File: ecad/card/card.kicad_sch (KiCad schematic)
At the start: 52 parts, among them J1 Conn_01x03_Pin, J2 USB4105-GF-A, SW1 SW_Push, SW2 SW_Push, U1 W25Q128JVS, U2 RP2350_80QFN, U3 MCP23017_SO, U4 NCP1117-3.3_SOT223, U5 MCP23017_SO, X1 ABM8-272-T3

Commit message: fixup card labels
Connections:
- net ADDR00: now also U2.25 (GPIO24)
- net ADDR01: now also U2.26 (GPIO25)
- net ADDR02: now also U2.27 (GPIO26)
- net ADDR03: now also U2.28 (GPIO27)
- net ADDR04: now also U2.36 (GPIO28)
- net ADDR05: now also U2.37 (GPIO29)
- net ADDR06: now also U2.38 (GPIO30)
- net ADDR07: now also U2.39 (GPIO31)
- net ADDR08: now also U2.40 (GPIO32)
- net ADDR09: now also U2.42 (GPIO33)
- net ADDR10: now also U2.43 (GPIO34)
- net ADDR11: now also U2.44 (GPIO35)
- net ADDR12: now also U2.45 (GPIO36)
- net ADDR13: now also U2.46 (GPIO37)
- net ADDR14: now also U2.47 (GPIO38)
- net ADDR15: now also U2.48 (GPIO39)
- net BUS00: now also U2.23 (GPIO23)
- net BUS01: now also U2.22 (GPIO22)
- net BUS02: now also U2.21 (GPIO21)
- net BUS03: now also U2.20 (GPIO20)
- net BUS04: now also U2.19 (GPIO19)
- net BUS05: now also U2.18 (GPIO18)
- net BUS06: now also U2.17 (GPIO17)
- net BUS07: now also U2.16 (GPIO16)
- net BUS08: now also U2.14 (GPIO15)
- net BUS09: now also U2.13 (GPIO14)
- net BUS10: now also U2.12 (GPIO13)
- net BUS11: now also U2.11 (GPIO12)
- net BUS12: now also U2.9 (GPIO11)
- net BUS13: now also U2.8 (GPIO10)
- net BUS14: now also U2.7 (GPIO9)
- net BUS15: now also U2.6 (GPIO8)
- net BUS16: now also U2.4 (GPIO7)
- net BUS17: now also U2.3 (GPIO6)
- net BUS18: now also U2.2 (GPIO5)
- net BUS19: now also U2.1 (GPIO4)
- net BUS20: now also JP1.2 (B)
- net BUS21: now also JP4.2 (B)
- net BUS22: now also JP6.2 (B)
- net BUS23: now also JP8.2 (B)
- net DATA0: now also U2.49 (GPIO40_ADC0)
- net DATA1: now also U2.52 (GPIO41_ADC1)
- net DATA2: now also U2.53 (GPIO42_ADC2)
- net DATA3: now also U2.54 (GPIO43_ADC3)
- net DATA4: now also U2.55 (GPIO44_ADC4)
- net DATA5: now also U2.56 (GPIO45_ADC5)
- net DATA6: now also U2.57 (GPIO46_ADC6)
- net DATA7: now also U2.58 (GPIO47_ADC7)
- net EXT00: now also U3.1 (GPB0)
- net EXT01: now also U3.2 (GPB1)
- net EXT02: now also U3.3 (GPB2)
- net EXT03: now also U3.4 (GPB3)
- net EXT04: now also U3.5 (GPB4)
- net EXT05: now also U3.6 (GPB5)
- net EXT06: now also U3.7 (GPB6)
- net EXT07: now also U3.8 (GPB7)
- net EXT08: now also U3.21 (GPA0)
- net EXT09: now also U3.22 (GPA1)
- net EXT10: now also U3.23 (GPA2)
- net EXT11: now also U3.24 (GPA3)
- net EXT12: now also U3.25 (GPA4)
- net EXT13: now also U3.26 (GPA5)
- net EXT14: now also U3.27 (GPA6)
- net EXT15: now also U3.28 (GPA7)
- net EXT16: now also U5.1 (GPB0)
- net EXT17: now also U5.2 (GPB1)
- net EXT18: now also U5.3 (GPB2)
- net EXT19: now also U5.4 (GPB3)
- net EXT20: now also U5.5 (GPB4)
- net EXT21: now also U5.6 (GPB5)
- net EXT22: now also U5.7 (GPB6)
- net EXT23: now also U5.8 (GPB7)
- net EXT24: now also U5.21 (GPA0)
- net EXT25: now also U5.22 (GPA1)
- net EXT26: now also U5.23 (GPA2)
- net EXT27: now also U5.24 (GPA3)
- net EXT28: now also U5.25 (GPA4)
- net EXT29: now also U5.26 (GPA5)
- net EXT30: now also U5.27 (GPA6)
- net EXT31: now also U5.28 (GPA7)
- net I2C0_SCL: now also JP5.2 (B), U3.12 (SCK)
- net I2C0_SDA: now also JP7.2 (B), U3.13 (SDA)
- net I2C1_SCL: now also JP2.2 (B), U5.12 (SCK)
- net I2C1_SDA: now also JP3.2 (B), U5.13 (SDA)
- net QSPI_SS: now also R3.2, U1.1 (~{CS}), U2.75 (QSPI_SS)
- net USB_D+: now also J2.A6 (DP1), J2.B6 (DP2), R5.2
- net USB_D-: now also J2.A7 (DN1), J2.B7 (DN2), R6.2
- net VREG_LX: now also L1.2, U2.63 (VREG_LX)
- net ~{RESET}: now also R7.1, SW2.2, U2.35 (RUN), U3.18 (~{RESET}), U5.18 (~{RESET})
- net ~{USB_BOOT}: now also R3.1, SW1.2
- net VREG_AVDD: now reaches C7.1, R2.2, U2.61 (VREG_AVDD)

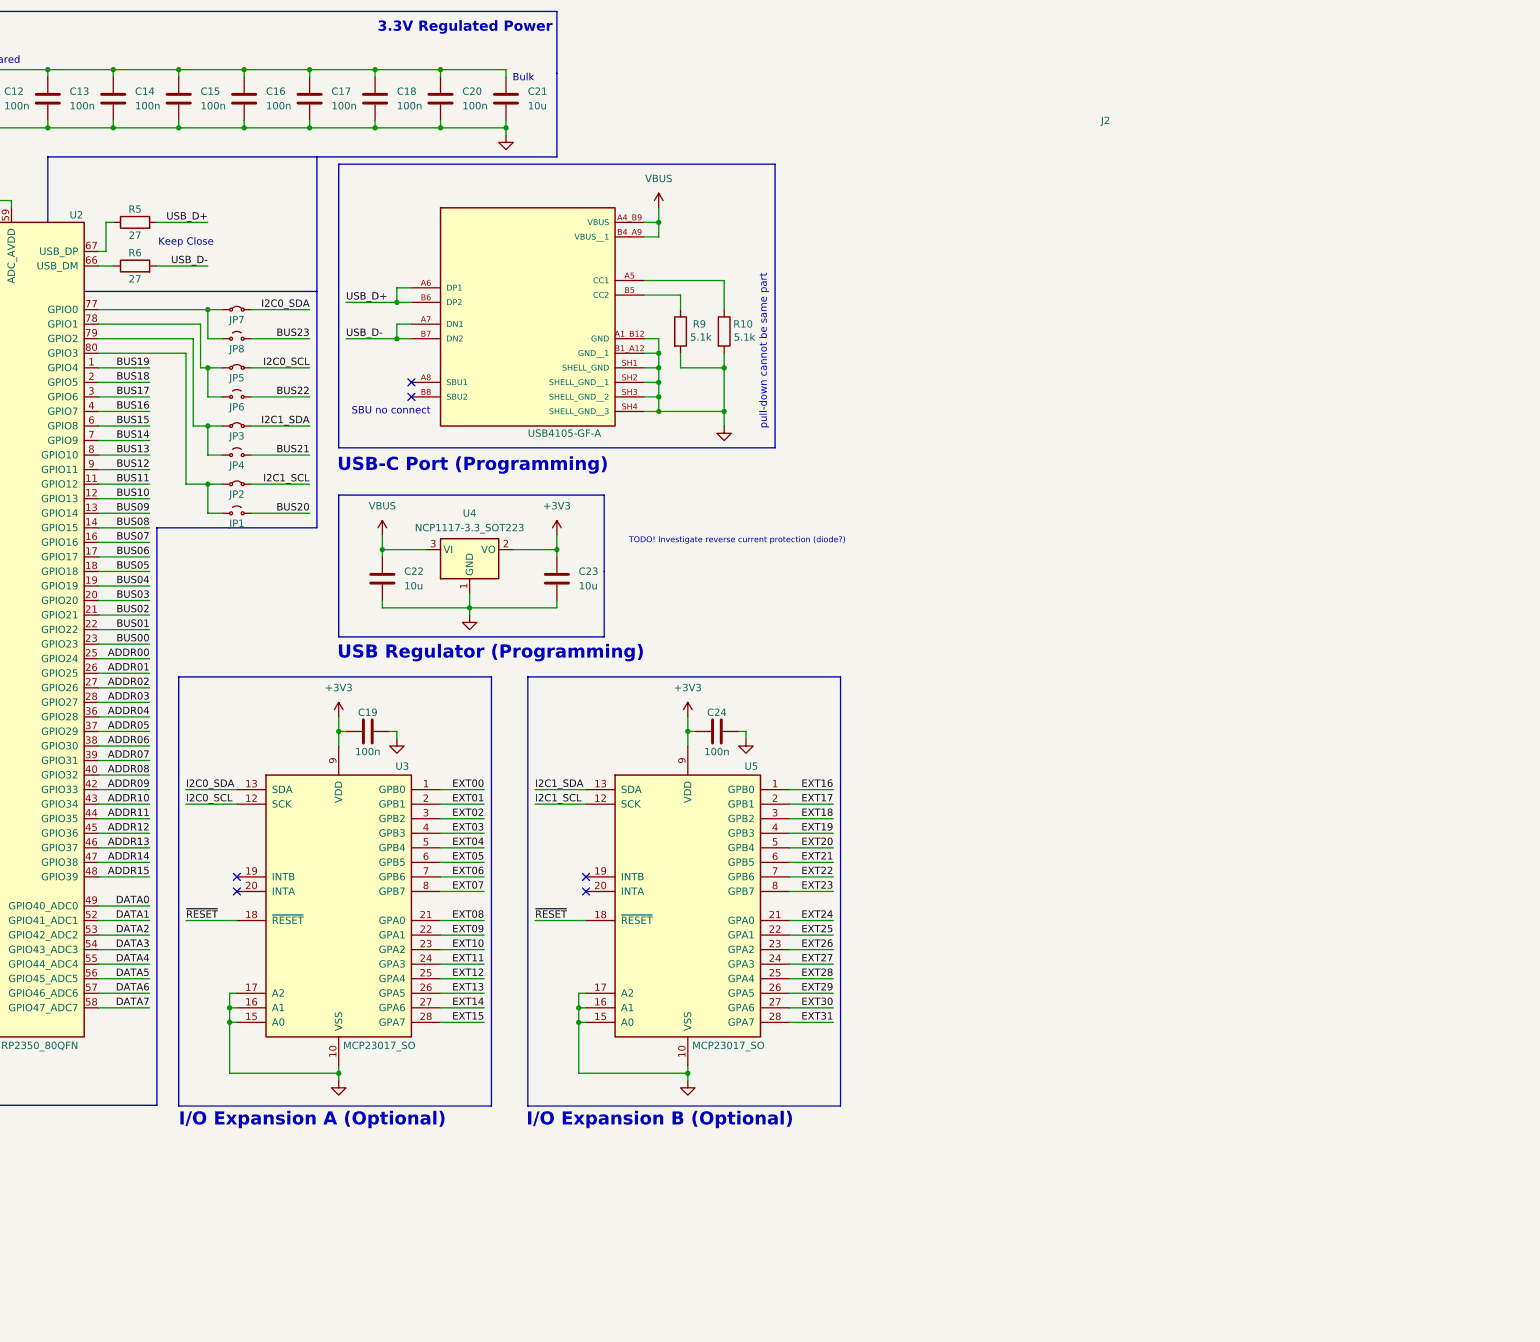
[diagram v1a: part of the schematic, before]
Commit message: integrate edge card symbol into card
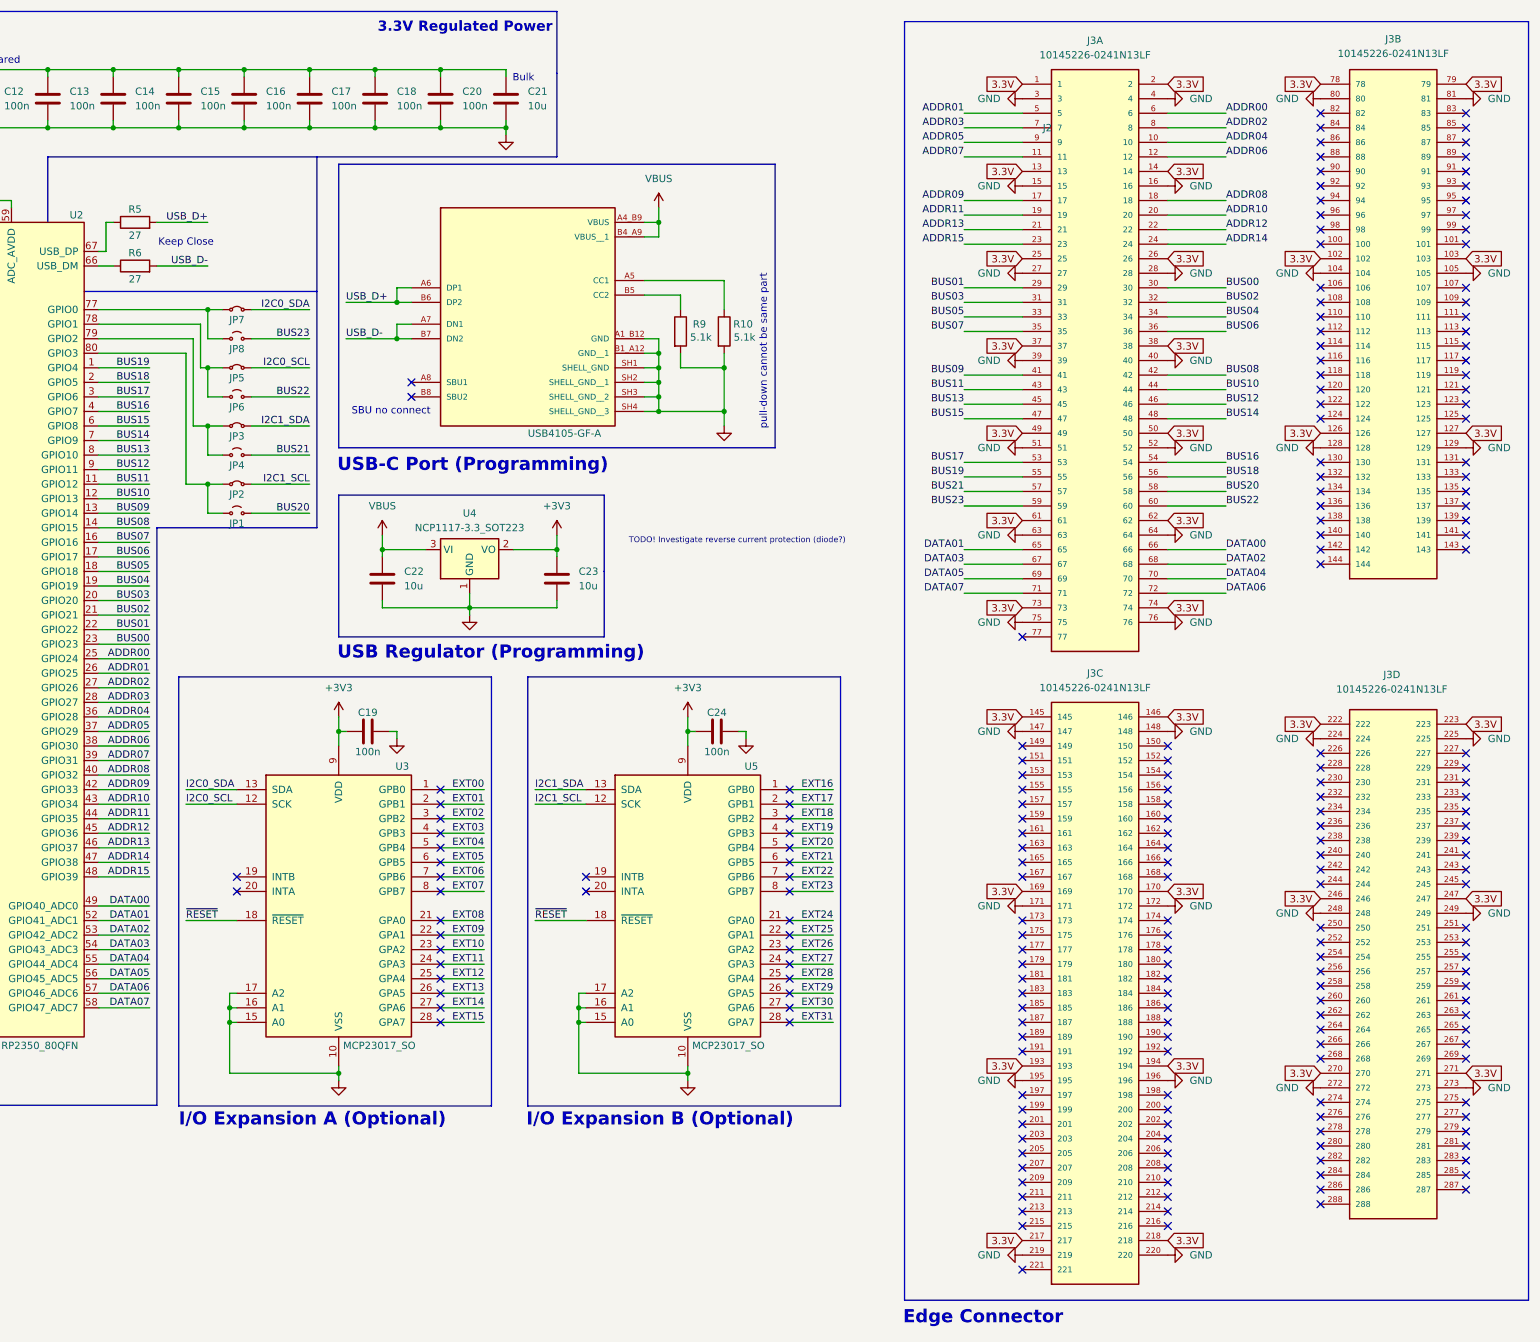
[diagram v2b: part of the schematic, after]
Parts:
- added J3: 10145226-0241N13LF, 10145226-0241N13LF:AMPHENOL_10145226-0241N13LF, symbol Project_Library:10145226-0241N13LF
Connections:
- net ADDR00: now also J3.6
- net ADDR01: now also J3.5
- net ADDR02: now also J3.8
- net ADDR03: now also J3.7
- net ADDR04: now also J3.10
- net ADDR05: now also J3.9
- net ADDR06: now also J3.12
- net ADDR07: now also J3.11
- net ADDR08: now also J3.18
- net ADDR09: now also J3.17
- net ADDR10: now also J3.20
- net ADDR11: now also J3.19
- net ADDR12: now also J3.22
- net ADDR13: now also J3.21
- net ADDR14: now also J3.24
- net ADDR15: now also J3.23
- net BUS00: now also J3.30
- net BUS01: now also J3.29
- net BUS02: now also J3.32
- net BUS03: now also J3.31
- net BUS04: now also J3.34
- net BUS05: now also J3.33
- net BUS06: now also J3.36
- net BUS07: now also J3.35
- net BUS08: now also J3.42
- net BUS09: now also J3.41
- net BUS10: now also J3.44
- net BUS11: now also J3.43
- net BUS12: now also J3.46
- net BUS13: now also J3.45
- net BUS14: now also J3.48
- net BUS15: now also J3.47
- net BUS16: now also J3.54
- net BUS17: now also J3.53
- net BUS18: now also J3.56
- net BUS19: now also J3.55
- net BUS20: now also J3.58
- net BUS21: now also J3.57
- net BUS22: now also J3.60
- net BUS23: now also J3.59
- net GND: now also J3.104, J3.105, J3.128, J3.129, J3.147, J3.148, J3.15, J3.16, J3.171, J3.172, J3.195, J3.196, J3.219, J3.220, J3.224, J3.225, J3.248, J3.249, J3.27, J3.272, J3.273, J3.28, J3.3, J3.39, J3.4, J3.40, J3.51, J3.52, J3.63, J3.64, J3.75, J3.76, J3.80, J3.81
- net DATA0 renamed DATA00
- net DATA00: now also J3.66
- net DATA1 renamed DATA01
- net DATA01: now also J3.65
- net DATA2 renamed DATA02
- net DATA02: now also J3.68
- net DATA3 renamed DATA03
- net DATA03: now also J3.67
- net DATA4 renamed DATA04
- net DATA04: now also J3.70
- net DATA5 renamed DATA05
- net DATA05: now also J3.69
- net DATA6 renamed DATA06
- net DATA06: now also J3.72
- net DATA7 renamed DATA07
- net DATA07: now also J3.71
- new net 3.3V: J3.1, J3.102, J3.103, J3.126, J3.127, J3.13, J3.14, J3.145, J3.146, J3.169, J3.170, J3.193, J3.194, J3.2, J3.217, J3.218, J3.222, J3.223, J3.246, J3.247, J3.25, J3.26, J3.270, J3.271, J3.37, J3.38, J3.49, J3.50, J3.61, J3.62, J3.73, J3.74, J3.78, J3.79
- no-connect marks 6 -> 210
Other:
- note added: "Edge Connector"

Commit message: card layout, lib updates
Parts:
- C1, C11, C12, C13, C14, C15, C16, C17, C18, C19, C2, C20, C21, C22, C23, C24, C3, C4, C6, C7, C8, C9: footprint (none) -> Capacitor_SMD:C_0402_1005Metric
- C10, C5: footprint (none) -> Capacitor_SMD:C_0603_1608Metric
- J1: footprint (none) -> Connector_JST:JST_XH_B3B-XH-AM_1x03_P2.50mm_Vertical
- J2: footprint USB4105-GF-A:GCT_USB4105-GF-A -> Library:GCT_USB4105-GF-A
- J3: footprint 10145226-0241N13LF:AMPHENOL_10145226-0241N13LF -> Library:DIMM-DDR4
- JP1, JP2, JP3, JP4, JP5, JP6, JP7, JP8: footprint (none) -> Resistor_SMD:R_0402_1005Metric_Pad0.72x0.64mm_HandSolder
- L1: footprint (none) -> Library:IND-SMD_L2.0-W1.6_AOTA-B201610S3R3-101-T; symbol Device:L -> Project_Library:AOTA-B201610S3R3-101-T; Manufacturer (none) -> ABRACON; Manufacturer Part (none) -> AOTA-B201610S3R3-101-T; Supplier (none) -> LCSC; Supplier Part (none) -> C42411119
- R1, R10, R2, R3, R4, R5, R6, R7, R9: footprint (none) -> Resistor_SMD:R_0402_1005Metric
- SW1, SW2: footprint (none) -> Button_Switch_SMD:SW_Push_1P1T_NO_Vertical_Wuerth_434133025816
- U2: footprint RP2350_80QFN_minimal:RP2350-QFN-80-1EP_10x10_P0.4mm_EP3.4x3.4mm_ThermalVias -> Library:RP2350-QFN-80-1EP_10x10_P0.4mm_EP3.4x3.4mm_ThermalVias
- X1: footprint ABM8-272-T3_ABR -> Library:ABM8-272-T3_ABR
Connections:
- net 3.3V is gone; now on net +3V3: J3.1, J3.102, J3.103, J3.126, J3.127, J3.13, J3.14, J3.145, J3.146, J3.169, J3.170, J3.193, J3.194, J3.2, J3.217, J3.218, J3.222, J3.223, J3.246, J3.247, J3.25, J3.26, J3.270, J3.271, J3.37, J3.38, J3.49, J3.50, J3.61, J3.62, J3.73, J3.74, J3.78, J3.79
- net +1V1: now also L1.2; no longer L1.1
- net VREG_LX: now also L1.1; no longer L1.2
- net VREG_AVDD: no longer names the net of C7.1, R2.2, U2.61 (VREG_AVDD)
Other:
- moved on the sheet: C2

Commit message: near-final card layout
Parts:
- added R11, R12, R13, R14, R15, R16, R17, R18, R19, R20, R21, R22, R23, R24, R25, R26, R27, R28, R29, R30, R31, R32, R33, R34, R35, R36, R37, R38, R39, R40, R41, R42, R43, R44, R45, R46, R47, R48, R49, R50, R51, R52, R53, R54, R55, R56, R57, R58, R59, R60, R61, R62, R63, R64, R65, R66, R67, R68, R69, R70, R71, R72, R73, R74, R75, R76, R77, R78, R79, R8, R80, R81, R82, R83, R84, R85, R86, R87, R88, R89: 330, Resistor_SMD:R_0402_1005Metric, symbol Device:R_Small
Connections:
- net +3V3: now also J3.114, J3.115, J3.138, J3.139, J3.157, J3.158, J3.181, J3.182, J3.205, J3.206, J3.234, J3.235, J3.258, J3.259, J3.282, J3.283, J3.90, J3.91
- net ADDR00: now also U2.16 (GPIO16), R26.1; no longer J3.6, U2.25 (GPIO24)
- net ADDR01: now also U2.17 (GPIO17), R27.1; no longer J3.5, U2.26 (GPIO25)
- net ADDR02: now also U2.18 (GPIO18), R28.1; no longer J3.8, U2.27 (GPIO26)
- net ADDR03: now also U2.19 (GPIO19), R29.1; no longer J3.7, U2.28 (GPIO27)
- net ADDR04: now also U2.20 (GPIO20), R30.1; no longer J3.10, U2.36 (GPIO28)
- net ADDR05: now also U2.21 (GPIO21), R31.1; no longer J3.9, U2.37 (GPIO29)
- net ADDR06: now also U2.22 (GPIO22), R32.1; no longer J3.12, U2.38 (GPIO30)
- net ADDR07: now also U2.23 (GPIO23), R33.1; no longer J3.11, U2.39 (GPIO31)
- net ADDR08: now also U2.25 (GPIO24), R34.1; no longer J3.18, U2.40 (GPIO32)
- net ADDR09: now also U2.26 (GPIO25), R35.1; no longer J3.17, U2.42 (GPIO33)
- net ADDR10: now also U2.27 (GPIO26), R36.1; no longer J3.20, U2.43 (GPIO34)
- net ADDR11: now also U2.28 (GPIO27), R37.1; no longer J3.19, U2.44 (GPIO35)
- net ADDR12: now also U2.36 (GPIO28), R38.1; no longer J3.22, U2.45 (GPIO36)
- net ADDR13: now also U2.37 (GPIO29), R39.1; no longer J3.21, U2.46 (GPIO37)
- net ADDR14: now also U2.38 (GPIO30), R40.1; no longer J3.24, U2.47 (GPIO38)
- net ADDR15: now also U2.39 (GPIO31), R41.1; no longer J3.23, U2.48 (GPIO39)
- net BUS05: now also J3.5, R13.2; no longer J3.33, U2.18 (GPIO18)
- net BUS06: now also J3.6, R12.2; no longer J3.36, U2.17 (GPIO17)
- net BUS07: now also J3.7, R14.2; no longer J3.35, U2.16 (GPIO16)
- net BUS08: now also J3.8, R15.2; no longer J3.42, U2.14 (GPIO15)
- net BUS09: now also J3.9, R11.2; no longer J3.41, U2.13 (GPIO14)
- net BUS10: now also J3.10, R16.2; no longer J3.44, U2.12 (GPIO13)
- net BUS11: now also J3.11, R17.2; no longer J3.43, U2.11 (GPIO12)
- net BUS12: now also J3.12, R8.2; no longer J3.46, U2.9 (GPIO11)
- net BUS17: now also J3.17, R18.2; no longer J3.53, U2.3 (GPIO6)
- net BUS18: now also J3.18, R19.2; no longer J3.56, U2.2 (GPIO5)
- net BUS19: now also J3.19, R20.2; no longer J3.55, U2.1 (GPIO4)
- net BUS20: now also J3.20, R21.2; no longer J3.58, JP1.2 (B)
- net BUS21: now also J3.21, R22.2; no longer J3.57, JP4.2 (B)
- net BUS22: now also J3.22, R23.2; no longer J3.60, JP6.2 (B)
- net BUS23: now also J3.23, R24.2; no longer J3.59, JP8.2 (B)
- net DATA00: now also U2.6 (GPIO8), R18.1; no longer J3.66, U2.49 (GPIO40_ADC0)
- net DATA01: now also U2.7 (GPIO9), R19.1; no longer J3.65, U2.52 (GPIO41_ADC1)
- net DATA02: now also U2.8 (GPIO10), R20.1; no longer J3.68, U2.53 (GPIO42_ADC2)
- net DATA03: now also U2.9 (GPIO11), R21.1; no longer J3.67, U2.54 (GPIO43_ADC3)
- net DATA04: now also U2.11 (GPIO12), R22.1; no longer J3.70, U2.55 (GPIO44_ADC4)
- net DATA05: now also U2.12 (GPIO13), R23.1; no longer J3.69, U2.56 (GPIO45_ADC5)
- net DATA06: now also U2.13 (GPIO14), R24.1; no longer J3.72, U2.57 (GPIO46_ADC6)
- net DATA07: now also U2.14 (GPIO15), R25.1; no longer J3.71, U2.58 (GPIO47_ADC7)
- net EXT00: now also R58.1
- net EXT01: now also R59.1
- net EXT02: now also R60.1
- net EXT03: now also R61.1
- net EXT04: now also R62.1
- net EXT05: now also R63.1
- net EXT06: now also R64.1
- net EXT07: now also R65.1
- net EXT08: now also R66.1
- net EXT09: now also R67.1
- net EXT10: now also R68.1
- net EXT11: now also R69.1
- net EXT12: now also R70.1
- net EXT13: now also R71.1
- net EXT14: now also R72.1
- net EXT15: now also R73.1
- net EXT16: now also R74.1
- net EXT17: now also R75.1
- net EXT18: now also R76.1
- net EXT19: now also R77.1
- net EXT20: now also R78.1
- net EXT21: now also R79.1
- net EXT22: now also R80.1
- net EXT23: now also R81.1
- net EXT24: now also R82.1
- net EXT25: now also R83.1
- net EXT26: now also R84.1
- net EXT27: now also R85.1
- net EXT28: now also R86.1
- net EXT29: now also R87.1
- net EXT30: now also R88.1
- net EXT31: now also R89.1
- net GND: now also J3.116, J3.117, J3.140, J3.141, J3.159, J3.160, J3.183, J3.184, J3.207, J3.208, J3.236, J3.237, J3.260, J3.261, J3.284, J3.285, J3.92, J3.93
- net I2C0_SCL: now also JP2.2 (B); no longer JP5.2 (B)
- net I2C0_SDA: now also JP3.2 (B); no longer JP7.2 (B)
- net I2C1_SCL: now also JP5.2 (B); no longer JP2.2 (B)
- net I2C1_SDA: now also JP7.2 (B); no longer JP3.2 (B)
- net JUMP1: now reaches JP3.1 (A), JP4.1 (A)
- net JUMP1: now also U2.55 (GPIO44_ADC4); no longer U2.79 (GPIO2)
- net JUMP3: now reaches JP7.1 (A), JP8.1 (A)
- net JUMP3: now also U2.53 (GPIO42_ADC2); no longer U2.77 (GPIO0)
- net JUMP2: now reaches JP5.1 (A), JP6.1 (A)
- net JUMP2: now also U2.54 (GPIO43_ADC3); no longer U2.78 (GPIO1)
- net JUMP0: now reaches JP1.1 (A), JP2.1 (A)
- net JUMP0: now also U2.56 (GPIO45_ADC5); no longer U2.80 (GPIO3)
- net BEX100: now reaches J3.100
- net BEX100: now also R72.2
- net BEX101: now reaches J3.101
- net BEX101: now also R73.2
- net BEX106: now reaches J3.106
- net BEX106: now also R74.2
- net BEX107: now reaches J3.107
- net BEX107: now also R75.2
- net BEX108: now reaches J3.108
- net BEX108: now also R76.2
- net BEX109: now reaches J3.109
- net BEX109: now also R77.2
- net BEX110: now reaches J3.110
- net BEX110: now also R78.2
- net BEX111: now reaches J3.111
- net BEX111: now also R79.2
- net BEX112: now reaches J3.112
- net BEX112: now also R80.2
- net BEX113: now reaches J3.113
- net BEX113: now also R81.2
- net BEX118: now reaches J3.118
- net BEX118: now also R82.2
- net BEX119: now reaches J3.119
- net BEX119: now also R83.2
- net BEX120: now reaches J3.120
- net BEX120: now also R84.2
- net BEX121: now reaches J3.121
- net BEX121: now also R85.2
- net BEX122: now reaches J3.122
- net BEX122: now also R86.2
- net BEX123: now reaches J3.123
- net BEX123: now also R87.2
- net BEX124: now reaches J3.124
- net BEX124: now also R88.2
- net BEX125: now reaches J3.125
- net BEX125: now also R89.2
- net BEX082: now reaches J3.82
- net BEX082: now also R58.2
- net BEX083: now reaches J3.83
- net BEX083: now also R59.2
- net BEX084: now reaches J3.84
- net BEX084: now also R60.2
- net BEX085: now reaches J3.85
- net BEX085: now also R61.2
- net BEX086: now reaches J3.86
- net BEX086: now also R62.2
- net BEX087: now reaches J3.87
- net BEX087: now also R63.2
- net BEX088: now reaches J3.88
- net BEX088: now also R64.2
- net BEX089: now reaches J3.89
- net BEX089: now also R65.2
- net BEX094: now reaches J3.94
- net BEX094: now also R66.2
- net BEX095: now reaches J3.95
- net BEX095: now also R67.2
- net BEX096: now reaches J3.96
- net BEX096: now also R68.2
- net BEX097: now reaches J3.97
- net BEX097: now also R69.2
- net BEX098: now reaches J3.98
- net BEX098: now also R70.2
- net BEX099: now reaches J3.99
- net BEX099: now also R71.2
- net BUS00 renamed BUS30
- net BUS30: now also R27.2; no longer U2.23 (GPIO23)
- net BUS01 renamed BUS29
- net BUS29: now also R26.2; no longer U2.22 (GPIO22)
- net BUS02 renamed BUS32
- net BUS32: now also R29.2; no longer U2.21 (GPIO21)
- net BUS03 renamed BUS31
- net BUS31: now also R28.2; no longer U2.20 (GPIO20)
- net BUS04 renamed BUS34
- net BUS34: now also R31.2; no longer U2.19 (GPIO19)
- net BUS13 renamed BUS45
- net BUS45: now also R36.2; no longer U2.8 (GPIO10)
- net BUS14 renamed BUS48
- net BUS48: now also R51.2; no longer U2.7 (GPIO9)
- net BUS15 renamed BUS47
- net BUS47: now also R37.2; no longer U2.6 (GPIO8)
- net BUS16 renamed BUS54
- net BUS54: now also R39.2; no longer U2.4 (GPIO7)
- new net BUS24: J3.24, R25.2
- new net BUS33: J3.33, R30.2
- new net BUS35: J3.35, R32.2
- new net BUS36: J3.36, R33.2
- new net BUS41: J3.41, R34.2
- new net BUS42: J3.42, R57.2
- new net BUS43: J3.43, R35.2
- new net BUS44: J3.44, R56.2
- new net BUS46: J3.46, R50.2
- new net BUS53: J3.53, R38.2
- new net BUS55: J3.55, R40.2
- new net BUS56: J3.56, R41.2
- new net BUS57: J3.57, R42.2
- new net BUS58: J3.58, R43.2
- new net BUS59: J3.59, R44.2
- new net BUS60: J3.60, R45.2
- new net BUS65: J3.65, R46.2
- new net BUS66: J3.66, R47.2
- new net BUS67: J3.67, R48.2
- new net BUS68: J3.68, R49.2
- new net BUS69: J3.69, R55.2
- new net BUS70: J3.70, R54.2
- new net BUS71: J3.71, R53.2
- new net BUS72: J3.72, R52.2
- new net CTRL00: R8.1, U2.77 (GPIO0)
- new net CTRL01: R11.1, U2.78 (GPIO1)
- new net CTRL02: R12.1, U2.79 (GPIO2)
- new net CTRL03: R13.1, U2.80 (GPIO3)
- new net CTRL04: R14.1, U2.1 (GPIO4)
- new net CTRL05: R15.1, U2.2 (GPIO5)
- new net CTRL06: R16.1, U2.3 (GPIO6)
- new net CTRL07: R17.1, U2.4 (GPIO7)
- new net CTRL08: R42.1, U2.40 (GPIO32)
- new net CTRL09: R43.1, U2.42 (GPIO33)
- new net CTRL10: R44.1, U2.43 (GPIO34)
- new net CTRL11: R45.1, U2.44 (GPIO35)
- new net CTRL12: R46.1, U2.45 (GPIO36)
- new net CTRL13: R47.1, U2.46 (GPIO37)
- new net CTRL14: R48.1, U2.47 (GPIO38)
- new net CTRL15: R49.1, U2.48 (GPIO39)
- new net CTRL16: R50.1, U2.49 (GPIO40_ADC0)
- new net CTRL17: R51.1, U2.52 (GPIO41_ADC1)
- new net CTRL18: R56.1, U2.57 (GPIO46_ADC6)
- new net CTRL19: R57.1, U2.58 (GPIO47_ADC7)
- new net CTRL20: JP8.2 (B), R52.1
- new net CTRL21: JP6.2 (B), R53.1
- new net CTRL22: JP4.2 (B), R54.1
- new net CTRL23: JP1.2 (B), R55.1
- no-connect marks 210 -> 110
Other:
- note added: "Protection R all 330 Ohms"
- moved on the sheet: C19, C22, C23, C24, J3A, J3B, J3C, J3D, JP1, JP2, JP3, JP4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
